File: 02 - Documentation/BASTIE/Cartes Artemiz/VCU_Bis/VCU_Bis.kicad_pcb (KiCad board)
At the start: 2 copper layers, 62.9 x 31.8 mm, 18 parts, among them J1 4P Droit 22-11-2042, J2 4P Droit 22-11-2042, J3 4P Droit 22-11-2042, J4 2P Droit 2-11-2022, U1 Alim LP TSR_0.5-2450

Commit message: Kicadlib + Modifs cartes
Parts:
- removed J2: 4P Droit 22-11-2042, EPSA_lib:MOLEX_22-11-2042
- removed R1: 120, EPSA_lib:RESC3216X70N
- removed R11: 820, EPSA_lib:RESC3216X70N
- removed R12: 390, EPSA_lib:RESC3216X70N
- added ?: , , F.Cu at (185.4, 71.8)
- added ?: , , F.Cu at (131.4, 62.2)
- added ?: , , F.Cu at (185.4, 48.9)
- added C1: C, Capacitor_THT:CP_Radial_D5.0mm_P2.00mm, F.Cu at (157.5, 52.4)
- added C2: 10n, EPSA_lib:CAPC2012X130N, F.Cu at (134.6, 54.6)
- added R2: 8k2, EPSA_lib:RESC3216X70N, F.Cu at (170.8, 65.4)
- added R3: 8k2, EPSA_lib:RESC3216X70N, F.Cu at (170.8, 71.8)
- R10, R4, R7: value 820 -> 3k9
- R13, R14, R5, R8: value 820 -> 8k2
- R15: value 390 -> 3k9
- R6, R9: value 390 -> 8k2
- moved R4 26.7 mm to (175.3, 69.2), turned to 180 degrees
- moved R10 18.1 mm to (153.0, 68.6), turned to 180 degrees
- moved R9 15.8 mm to (148.6, 71.8), turned to 90 degrees
- moved R5 12.8 mm to (160.0, 65.4)
- moved R8 12.8 mm to (148.6, 65.4)
- moved R6 6.85 mm to (159.4, 71.8), turned to 90 degrees
- moved R14 6.66 mm to (181.6, 64.8)
- moved R13 6.66 mm to (181.6, 58.4)
- moved R7 6.54 mm to (164.5, 69.8), turned to 180 degrees
- moved J1 6.25 mm to (168.9, 53.3)
- moved R15 6.08 mm to (185.7, 62.2)
- moved J3 5.12 mm to (139.7, 69.2)
- moved J4 3.81 mm to (134.6, 50.8)
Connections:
- R10 pad 1: /Int AIR+ -> /Int VCU Pre
- R10 pad 2: +5V -> /Int Pre
- R4 pad 1: /Int Pre -> /Int VCU AIR+
- R4 pad 2: +5V -> /Int AIR+
- R5 pad 1: GND -> /Int Dis
- R5 pad 2: /Int Pre -> +5V
- R6 pad 1: /Int VCU Pre -> GND
- R6 pad 2: /Int Pre -> /Int Dis
- R7 pad 1: /Int Dis -> /Int VCU Dis
- R7 pad 2: +5V -> /Int Dis
- R8 pad 1: GND -> /Int Pre
- R8 pad 2: /Int Dis -> +5V
- R9 pad 1: /Int VCU Dis -> GND
- R9 pad 2: /Int Dis -> /Int Pre
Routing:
- net GND: track 96.0 -> 0.05 mm, vias 2 -> 0
- net /CAN H: track 20.2 -> 0.00 mm
- net +12V: track 9.63 -> 24.6 mm
- net +5V: track 49.6 -> 61.6 mm
- net /CAN L: track 11.9 -> 0.00 mm
- net /Int Pre: track 43.7 -> 36.9 mm
- net /Int VCU Dis: track 34.2 -> 28.7 mm
- net /Int VCU AIR+: track 48.5 -> 43.1 mm
- net /Int VCU Pre: track 21.8 -> 17.0 mm
- net /Int AIR+: track 31.5 -> 26.8 mm
- net /Int Dis: track 34.2 -> 29.8 mm
- net /Int AIR-: track 28.0 -> 24.1 mm
- net /Int VCU AIR-: track 57.9 -> 54.8 mm
- added copper zone on F.Cu, net GND
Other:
- board text added: "VCU Bis v1.0 EPSA"
- board text removed: "VCU Bis v1.0"

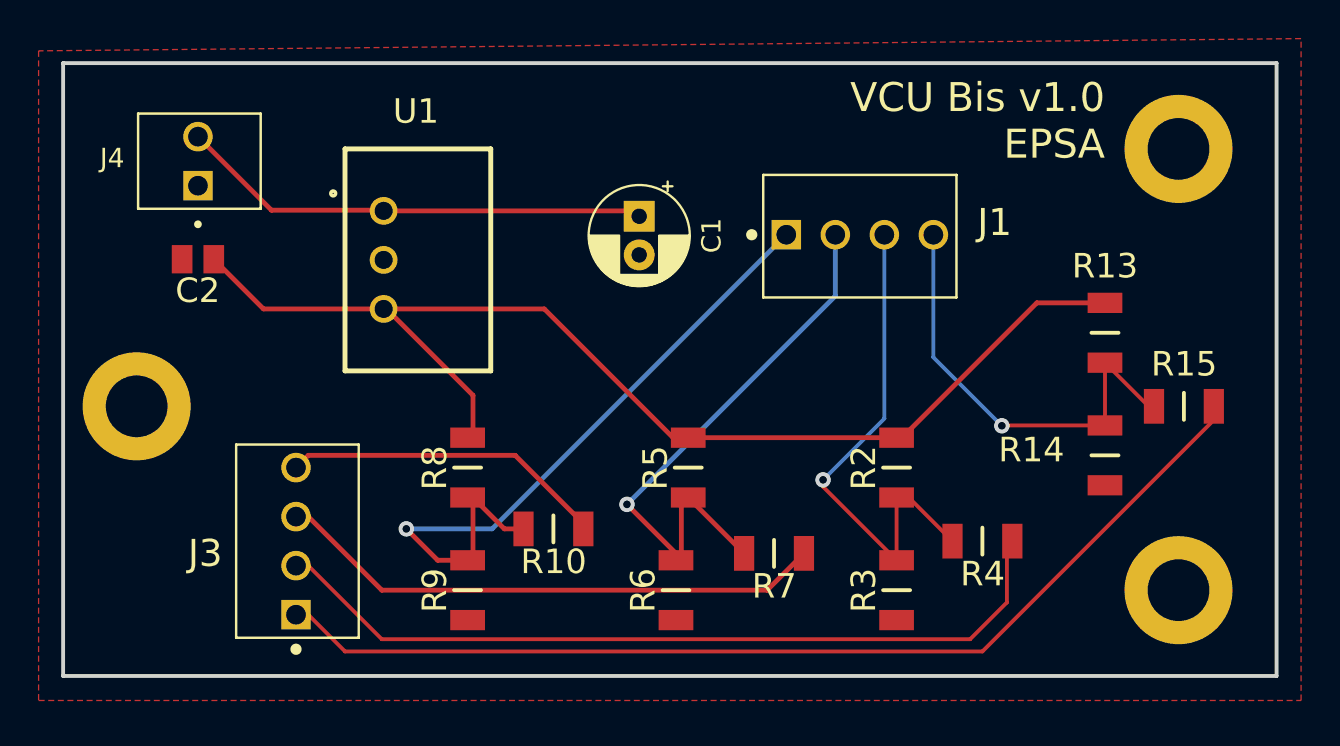
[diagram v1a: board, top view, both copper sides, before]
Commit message: Vérification PCBs + Fichiers Fabrication
Préparation pour production des PCBs
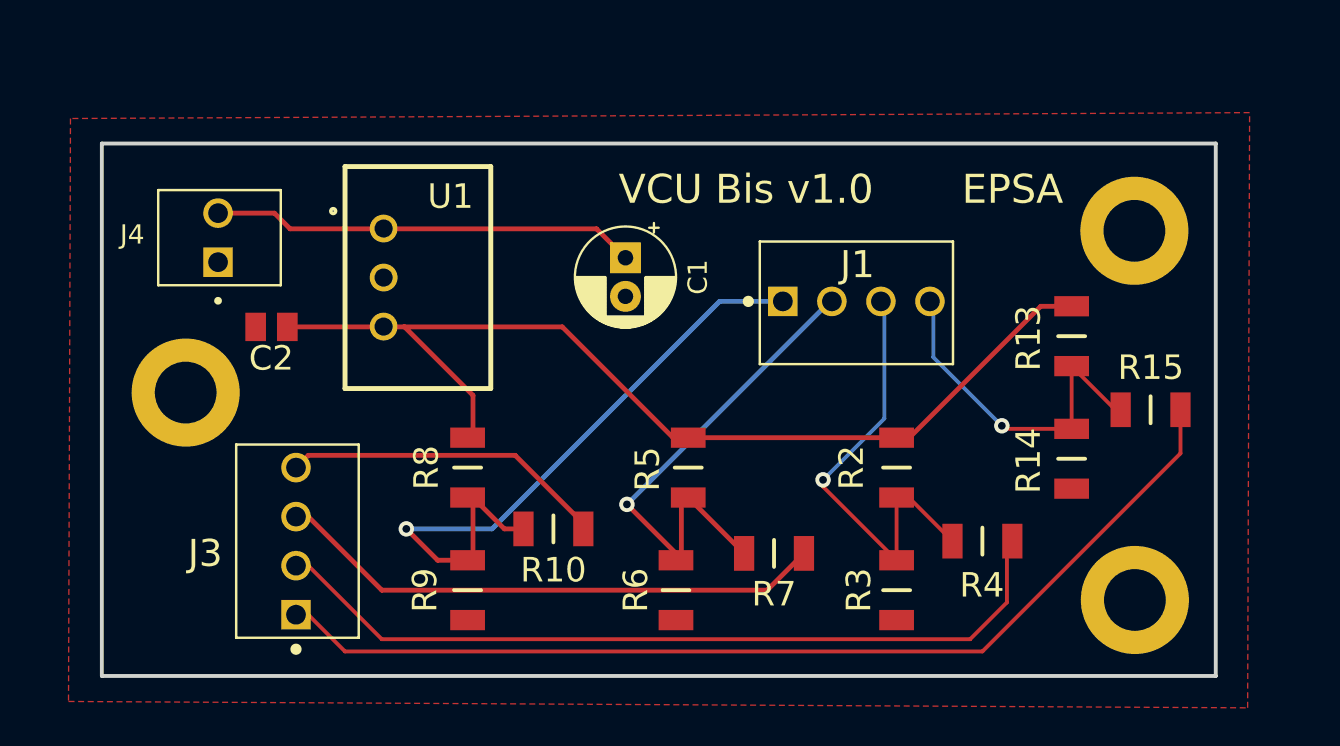
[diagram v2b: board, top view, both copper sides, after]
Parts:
- moved C2 5.18 mm to (138.4, 58.1)
- moved ? 4.82 mm to (183.1, 53.1)
- moved J4 4.10 mm to (135.7, 54.8)
- moved J1 3.46 mm to (168.7, 56.8)
- moved ? 2.64 mm to (134.0, 61.5)
- moved ? 2.32 mm to (183.2, 72.3)
- moved C1 2.26 mm to (156.8, 54.5)
- moved R13 1.74 mm to (179.9, 58.6)
- moved R14 1.74 mm to (179.9, 64.9)
- moved R15 1.74 mm to (184.0, 62.4)
- moved U1 0.91 mm to (142.2, 49.8)
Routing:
- net +5V: track 61.6 -> 53.1 mm
- net /Int AIR-: track 24.1 -> 19.0 mm
- net /Int Dis: track 29.8 -> 26.4 mm
- net /Int AIR+: track 26.8 -> 23.5 mm
- net +12V: track 24.6 -> 22.1 mm
- net /Int Pre: track 36.9 -> 35.3 mm
- net /Int VCU AIR-: track 54.8 -> 54.1 mm
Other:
- board size 62.9 x 31.8 mm -> 57.7 x 27.6 mm

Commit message: VC bis Led rounded corner + DRC ok
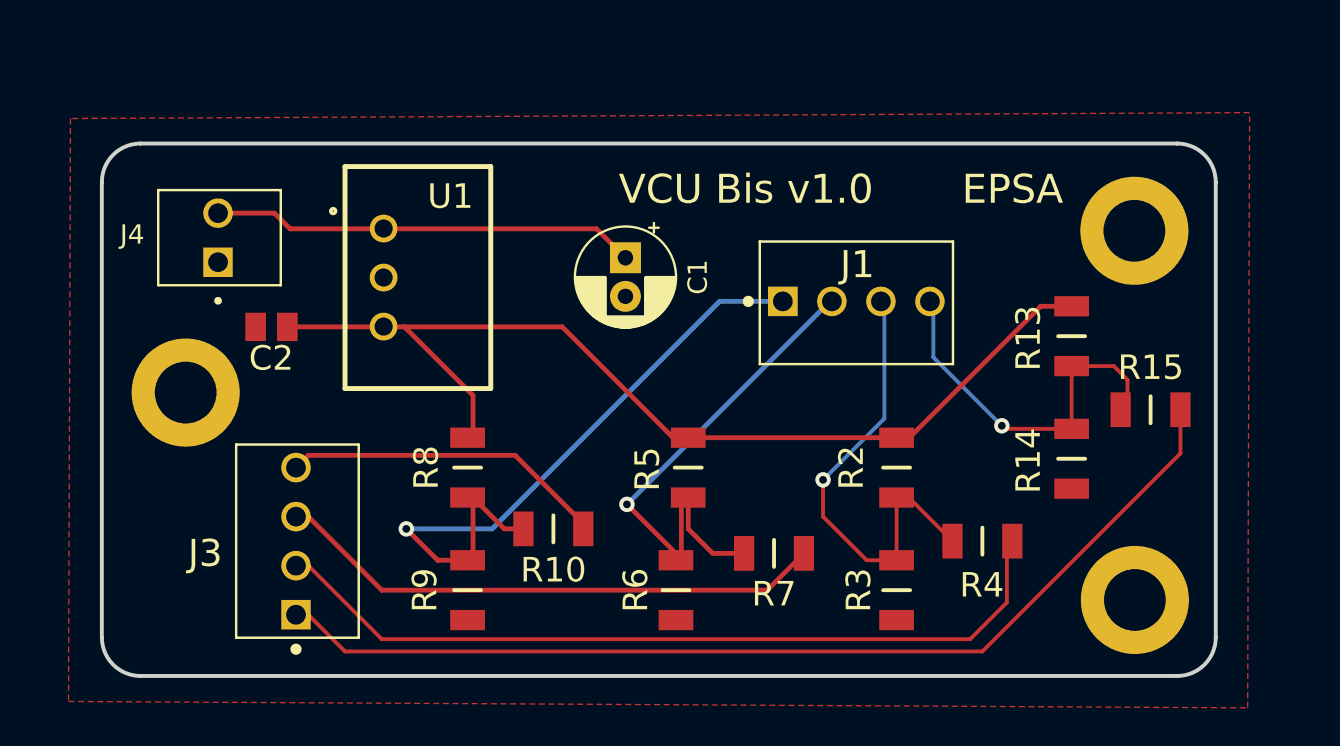
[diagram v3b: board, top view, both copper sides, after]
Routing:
- net /Int Dis: track 26.4 -> 27.3 mm
- net /Int AIR+: track 23.5 -> 24.4 mm
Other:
- outline, holes or cut-outs redrawn
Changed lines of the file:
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@@
 		)
 	)
-	(gr_rect
-		(start 129.6416 48.6156)
-		(end 187.3504 76.2)
-		(stroke
-			(width 0.2)
-			(type default)
-		)
-		(fill none)
+	(gr_line
+		(start 187.3504 50.6156)
+		(end 187.3504 74.2)
+		(stroke
+			(width 0.2)
+			(type default)
+		)
+		(layer "Edge.Cuts")
+	)
+	(gr_line
+		(start 131.6416 48.6156)
+		(end 185.3504 48.6156)
+		(stroke
+			(width 0.2)
+			(type default)
+		)
+		(layer "Edge.Cuts")
+	)
+	(gr_arc
+		(start 185.3504 48.6156)
+		(mid 186.764614 49.201386)
+		(end 187.3504 50.6156)
+		(stroke
+			(width 0.2)
+			(type default)
+		)
+		(layer "Edge.Cuts")
+	)
+	(gr_arc
+		(start 131.6416 76.2)
+		(mid 130.227386 75.614214)
+		(end 129.6416 74.2)
+		(stroke
+			(width 0.2)
+			(type default)
+		)
+		(layer "Edge.Cuts")
+	)
+	(gr_line
+		(start 129.6416 74.2)
+		(end 129.6416 50.6156)
+		(stroke
+			(width 0.2)
+			(type default)
+		)
+		(layer "Edge.Cuts")
+	)
+	(gr_line
+		(start 185.3504 76.2)
+		(end 131.6416 76.2)
+		(stroke
+			(width 0.2)
+			(type default)
+		)
+		(layer "Edge.Cuts")
+	)
+	(gr_arc
+		(start 187.3504 74.2)
+		(mid 186.764614 75.614214)
+		(end 185.3504 76.2)
+		(stroke
+			(width 0.2)
+			(type default)
+		)
+		(layer "Edge.Cuts")
+	)
+	(gr_arc
+		(start 129.6416 50.6156)
+		(mid 130.227386 49.201386)
+		(end 131.6416 48.6156)
+		(stroke
+			(width 0.2)
+			(type default)
+		)
 		(layer "Edge.Cuts")
 	)
@@
 	)
 	(segment
+		(start 182.0672 60.1472)
+		(end 179.8828 60.1472)
+		(width 0.2)
+		(layer "F.Cu")
+		(net 1)
+	)
+	(segment
 		(start 182.7778 61.7722)
-		(end 182.1428 62.4072)
+		(end 182.7778 60.8578)
 		(width 0.2)
 		(layer "F.Cu")
@@
 	)
 	(segment
-		(start 182.1428 62.4072)
-		(end 179.8828 60.1472)
-		(width 0.2)
-		(layer "F.Cu")
-		(net 1)
-	)
-	(segment
 		(start 176.4272 63.3972)
 		(end 179.8828 63.3972)
+		(width 0.2)
+		(layer "F.Cu")
+		(net 1)
+	)
+	(segment
+		(start 182.7778 60.8578)
+		(end 182.0672 60.1472)
 		(width 0.2)
 		(layer "F.Cu")
@@
 	)
 	(segment
-		(start 167.005 66.395)
-		(end 167.005 66.04)
-		(width 0.2)
-		(layer "F.Cu")
-		(net 2)
-	)
-	(segment
-		(start 170.815 70.205)
-		(end 167.005 66.395)
+		(start 169.265 70.205)
+		(end 167.005 67.945)
 		(width 0.2)
 		(layer "F.Cu")
@@
 	)
 	(segment
+		(start 167.005 67.945)
+		(end 167.005 66.04)
+		(width 0.2)
+		(layer "F.Cu")
+		(net 2)
+	)
+	(segment
 		(start 170.815 66.955)
 		(end 171.45 66.955)
+		(width 0.2)
+		(layer "F.Cu")
+		(net 2)
+	)
+	(segment
+		(start 170.815 70.205)
+		(end 169.265 70.205)
 		(width 0.2)
 		(layer "F.Cu")
@@
 	)
 	(segment
+		(start 161.29 69.85)
+		(end 162.915 69.85)
+		(width 0.25)
+		(layer "F.Cu")
+		(net 3)
+	)
+	(segment
+		(start 160.02 68.58)
+		(end 161.29 69.85)
+		(width 0.25)
+		(layer "F.Cu")
+		(net 3)
+	)
+	(segment
 		(start 160.02 66.955)
-		(end 162.915 69.85)
-		(width 0.25)
-		(layer "F.Cu")
+		(end 160.02 68.58)
+		(width 0.25)
+		(layer "F.Cu")
